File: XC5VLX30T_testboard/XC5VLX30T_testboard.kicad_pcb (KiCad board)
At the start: 4 copper layers, 15 parts, among them J1 Conn_02x30_Counter_Clockwise, J2 Conn_02x30_Counter_Clockwise, J3 Conn_02x30_Counter_Clockwise, J4 Conn_02x30_Counter_Clockwise, U1 XC5VLX30T-1FFG665C, X1 SG-5032CCN

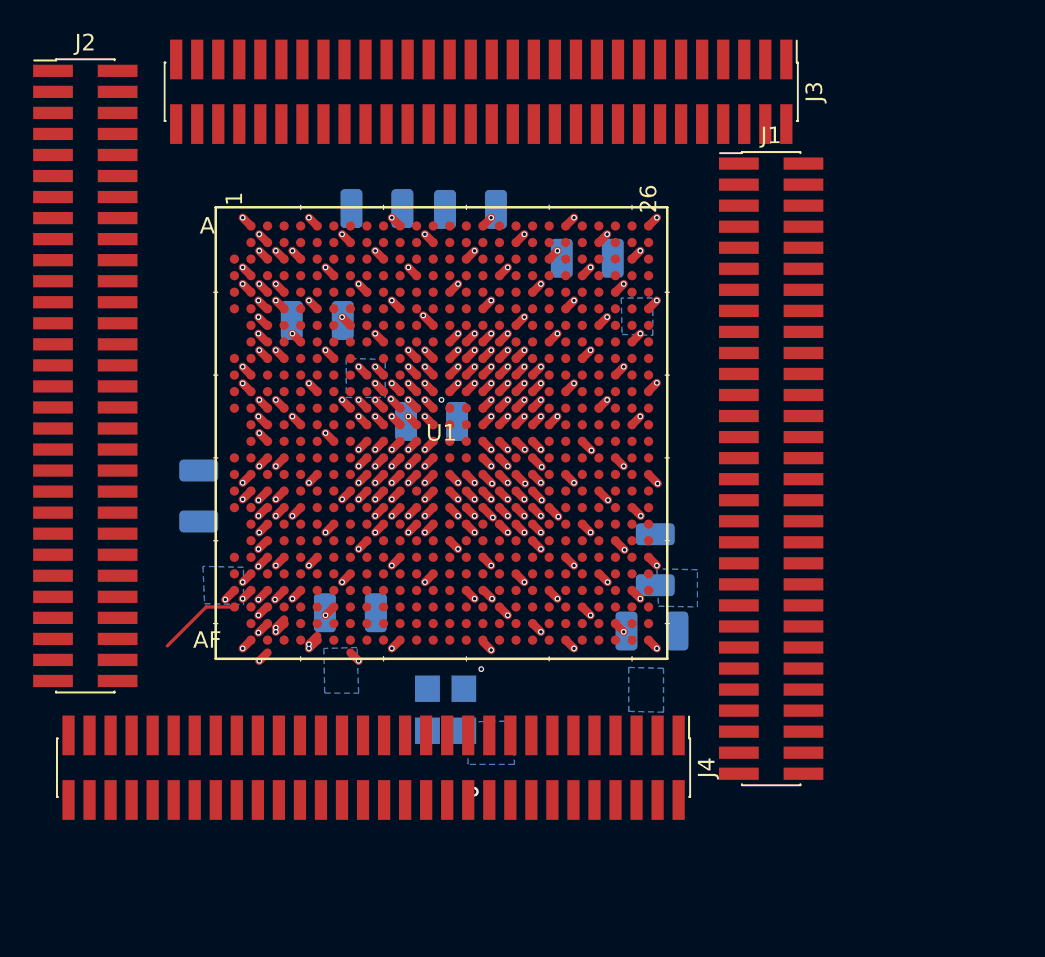
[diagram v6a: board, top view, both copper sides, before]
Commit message: routing
routed 240 pins on 4 layer
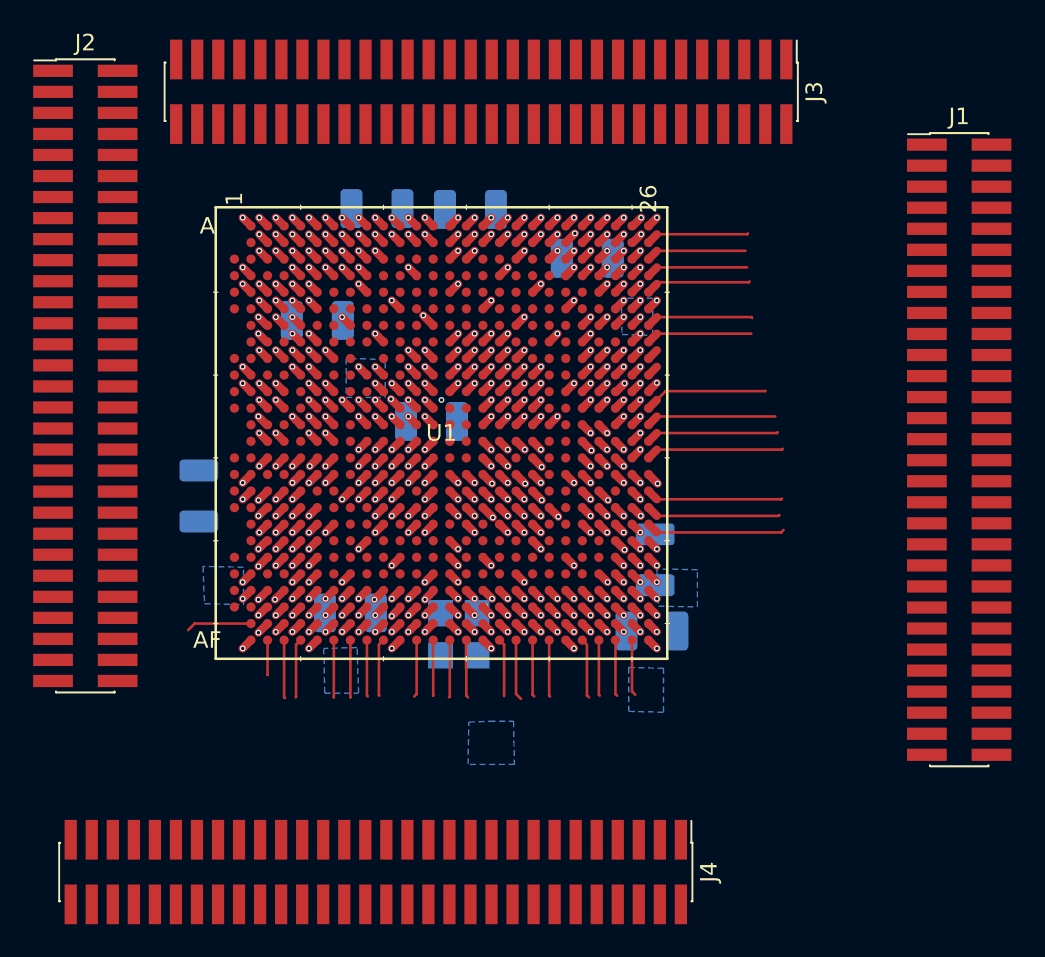
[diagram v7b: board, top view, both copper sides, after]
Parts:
- moved J1 11.4 mm to (192.9, 145.0)
- moved J4 6.30 mm to (157.7, 170.5)
- moved X1 4.62 mm to (162.7, 156.2)
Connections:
- U1 pad AC1: GND -> unconnected-(U1C-MGTRXN1_118-PadAC1)
- U1 pad AE10: unconnected-(U1G-IO_L4N_VREF_18-PadAE10) -> IO_L4N_VREF_18
- U1 pad AE11: unconnected-(U1G-IO_L2P_18-PadAE11) -> IO_L2P_18
- U1 pad AE12: unconnected-(U1G-IO_L0N_18-PadAE12) -> IO_L0N_18
- U1 pad AE13: unconnected-(U1G-IO_L18N_17-PadAE13) -> IO_L18N_17
- U1 pad AE15: unconnected-(U1G-IO_L16N_17-PadAE15) -> IO_L16N_17
- U1 pad AE16: unconnected-(U1G-IO_L15P_17-PadAE16) -> IO_L15P_17
- U1 pad AE17: unconnected-(U1G-IO_L14P_17-PadAE17) -> IO_L14P_17
- U1 pad AE18: unconnected-(U1G-IO_L13P_17-PadAE18) -> IO_L13P_17
- U1 pad AE20: unconnected-(U1G-IO_L9N_CC_17-PadAE20) -> IO_L9N_CC_17
- U1 pad AE21: unconnected-(U1G-IO_L8N_CC_17-PadAE21) -> IO_L8N_CC_17
- U1 pad AE22: unconnected-(U1G-IO_L5P_17-PadAE22) -> IO_L5P_17
- U1 pad AE23: unconnected-(U1G-IO_L4N_VREF_17-PadAE23) -> IO_L4N_VREF_17
- U1 pad AE25: unconnected-(U1G-IO_L2P_17-PadAE25) -> IO_L2P_17
- U1 pad AE26: unconnected-(U1G-IO_L2N_17-PadAE26) -> IO_L2N_17
- U1 pad AE5: unconnected-(U1C-IO_L14P_18-PadAE5) -> IO_L14P_18
- U1 pad AE6: unconnected-(U1C-IO_L13P_18-PadAE6) -> IO_L13P_18
- U1 pad AE7: unconnected-(U1C-IO_L11N_CC_18-PadAE7) -> IO_L11N_CC_18
- U1 pad AE8: unconnected-(U1C-IO_L11P_CC_18-PadAE8) -> IO_L11P_CC_18
- U1 pad AF10: unconnected-(U1G-IO_L6N_18-PadAF10) -> IO_L6N_18
- U1 pad AF12: unconnected-(U1G-IO_L0P_18-PadAF12) -> IO_L0P_18
- U1 pad AF13: unconnected-(U1G-IO_L18P_17-PadAF13) -> IO_L0P_17
- U1 pad AF14: unconnected-(U1G-IO_L17N_17-PadAF14) -> IO_L17N_17
- U1 pad AF15: unconnected-(U1G-IO_L17P_17-PadAF15) -> IO_L17P_17
- U1 pad AF17: unconnected-(U1G-IO_L14N_VREF_17-PadAF17) -> IO_L14N_VREF_17
- U1 pad AF18: unconnected-(U1G-IO_L12N_VRP_17-PadAF18) -> IO_L12N_VRP_17
- U1 pad AF19: unconnected-(U1G-IO_L12P_VRN_17-PadAF19) -> IO_L12P_VRN_17
- U1 pad AF20: unconnected-(U1G-IO_L9P_CC_17-PadAF20) -> IO_L9P_CC_17
- U1 pad AF22: unconnected-(U1G-IO_L8P_CC_17-PadAF22) -> IO_L8P_CC_17
- U1 pad AF23: unconnected-(U1G-IO_L4P_17-PadAF23) -> IO_L4P_17
- U1 pad AF24: unconnected-(U1G-IO_L3N_17-PadAF24) -> IO_L3N_17
- U1 pad AF25: unconnected-(U1G-IO_L3P_17-PadAF25) -> IO_L3P_17
- U1 pad AF3: unconnected-(U1C-IO_L15N_18-PadAF3) -> IO_L15N_18
- U1 pad AF4: unconnected-(U1C-IO_L15P_18-PadAF4) -> IO_L15P_18
- U1 pad AF5: unconnected-(U1C-IO_L13N_18-PadAF5) -> IO_L13N_18
- U1 pad AF7: unconnected-(U1C-IO_L8P_CC_18-PadAF7) -> IO_L8P_CC_18
- U1 pad AF8: unconnected-(U1C-IO_L8N_CC_18-PadAF8) -> IO_L8N_CC_18
- U1 pad AF9: unconnected-(U1C-IO_L6P_18-PadAF9) -> IO_L6P_18
- U1 pad F2: unconnected-(U1A-MGTTXN1_116-PadF2) -> GND
- U1 pad L3: unconnected-(U1A-MGTAVCC_112-PadL3) -> VccINT
- U1 pad L4: unconnected-(U1A-MGTAVCC_112-PadL4) -> VccINT
- U1 pad P5: GND -> unconnected-(U1B-MGTAVTTRXC-PadP5)
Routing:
- net VCCO: track 31.8 -> 134.5 mm
- net unconnected-(U1F-IO_L5N_SM4N_13-PadT25): track 0.00 -> 46.7 mm, vias 0 -> 5
- net unconnected-(U1B-IO_L8N_CC_12-PadT8): track 0.00 -> 41.3 mm, vias 0 -> 5
- net unconnected-(U1F-IO_L4P_13-PadU26): track 0.00 -> 24.8 mm, vias 0 -> 1
- net unconnected-(U1C-IO_L16N_15-PadC24): track 0.00 -> 20.2 mm, vias 0 -> 2
- net unconnected-(U1E-IO_L2P_SM6P_13-PadP24): track 0.00 -> 16.0 mm, vias 0 -> 2
- net unconnected-(U1D-IO_L16P_15-PadD24): track 0.00 -> 15.3 mm, vias 0 -> 2
- net unconnected-(U1F-IO_L8P_CC_SM1P_13-PadW26): track 0.00 -> 15.3 mm
- net unconnected-(U1F-IO_L4N_VREF_13-PadV26): track 0.00 -> 15.0 mm, vias 0 -> 1
- net unconnected-(U1C-IO_L12N_VRP_18-PadAD5): track 0.00 -> 14.5 mm, vias 0 -> 1
- net unconnected-(U1F-IO_L0N_SM8N_13-PadR26): track 0.00 -> 14.2 mm
- net unconnected-(U1E-IO_L0P_SM8P_13-PadP26): track 0.00 -> 13.8 mm
- net unconnected-(U1E-IO_L16P_SM12P_11-PadN26): track 0.00 -> 13.0 mm
- net unconnected-(U1E-IO_L16N_SM12N_11-PadM26): track 0.00 -> 12.9 mm
- net unconnected-(U1C-IO_L9N_CC_18-PadAB5): track 0.00 -> 12.5 mm, vias 0 -> 1
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- removed copper zone on In1.Cu, net VCCO
- removed copper zone on In1.Cu, net VccINT

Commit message: plumbing
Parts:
- added J5: Conn_01x35_Pin, Connector_PinHeader_1.27mm:PinHeader_1x35_P1.27mm_Vertical, F.Cu at (212.8, 102.6)
- added J6: Conn_01x35_Pin, Connector_PinHeader_1.27mm:PinHeader_1x35_P1.27mm_Vertical, F.Cu at (212.8, 148.2)
- added J7: Conn_01x35_Pin, Connector_PinHeader_1.27mm:PinHeader_1x35_P1.27mm_Vertical, F.Cu at (164.6, 193.1)
- added J8: Conn_01x35_Pin, Connector_PinHeader_1.27mm:PinHeader_1x35_P1.27mm_Vertical, F.Cu at (210.2, 193.0)
- J1, J2, J3, J4: value Conn_02x30_Counter_Clockwise -> Conn_01x35_Pin; footprint Connector_PinHeader_1.27mm:PinHeader_2x30_P1.27mm_Vertical_SMD -> Connector_PinHeader_1.27mm:PinHeader_1x35_P1.27mm_Vertical
- moved J1 86.1 mm to (118.2, 102.0)
- moved J4 71.6 mm to (167.1, 99.5), turned to 90 degrees
- moved J3 48.7 mm to (121.6, 99.5), turned to 90 degrees
- moved J2 23.0 mm to (118.3, 147.6)
- moved U1 4.13 mm to (164.4, 147.1)
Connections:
- J3 pad 2: unconnected-(J3-Pin_2-Pad2) -> J5PIN1
- J3 pad 3: unconnected-(J3-Pin_3-Pad3) -> J5PIN1
- J3 pad 4: unconnected-(J3-Pin_4-Pad4) -> J5PIN1
- J3 pad 5: unconnected-(J3-Pin_5-Pad5) -> IO_L14P_16
- J3 pad 6: unconnected-(J3-Pin_6-Pad6) -> IO_L14P_16
- U1 pad A4: unconnected-(U1A-IO_L14P_16-PadA4) -> IO_L14P_16
- U1 pad AA16: VCCO -> unconnected-(U1F-IO_L4P_13-PadU26)
- U1 pad AA6: VCCO -> unconnected-(U1F-IO_L4P_13-PadU26)
- U1 pad AB13: VCCO -> unconnected-(U1F-IO_L4P_13-PadU26)
- U1 pad AB23: VCCO -> unconnected-(U1F-IO_L4P_13-PadU26)
- U1 pad AC10: VCCO -> unconnected-(U1F-IO_L4P_13-PadU26)
- U1 pad AC20: VCCO -> unconnected-(U1F-IO_L4P_13-PadU26)
- U1 pad B13: VCCO -> unconnected-(U1F-IO_L4P_13-PadU26)
- U1 pad B23: VCCO -> unconnected-(U1F-IO_L4P_13-PadU26)
- U1 pad B4: unconnected-(U1A-IO_L16P_16-PadB4) -> IO_L16P_16
- U1 pad C10: VCCO -> unconnected-(U1F-IO_L4P_13-PadU26)
- U1 pad C23: unconnected-(U1C-IO_L15N_15-PadC23) -> unconnected-(U1F-IO_L4P_13-PadU26)
- U1 pad D17: VCCO -> unconnected-(U1F-IO_L4P_13-PadU26)
- U1 pad D23: unconnected-(U1D-IO_L12P_VRN_15-PadD23) -> unconnected-(U1F-IO_L4P_13-PadU26)
- U1 pad D7: VCCO -> unconnected-(U1F-IO_L4P_13-PadU26)
- U1 pad E14: VCCO -> unconnected-(U1F-IO_L4P_13-PadU26)
- U1 pad E24: VCCO -> unconnected-(U1F-IO_L4P_13-PadU26)
- U1 pad E6: unconnected-(U1A-IO_L7P_16-PadE6) -> IO_L7P_16
- U1 pad F11: VCCO -> unconnected-(U1F-IO_L4P_13-PadU26)
- U1 pad F21: VCCO -> unconnected-(U1F-IO_L4P_13-PadU26)
- U1 pad G18: VCCO -> unconnected-(U1F-IO_L4P_13-PadU26)
- U1 pad G8: VCCO -> unconnected-(U1F-IO_L4P_13-PadU26)
- U1 pad H25: VCCO -> unconnected-(U1F-IO_L4P_13-PadU26)
- U1 pad H5: VCCO -> unconnected-(U1F-IO_L4P_13-PadU26)
- U1 pad H6: unconnected-(U1A-IO_L1N_12-PadH6) -> unconnected-(U1F-IO_L4P_13-PadU26)
- U1 pad J12: VCCO -> unconnected-(U1F-IO_L4P_13-PadU26)
- U1 pad J22: VCCO -> unconnected-(U1F-IO_L4P_13-PadU26)
- U1 pad J6: unconnected-(U1A-IO_L7N_12-PadJ6) -> unconnected-(U1F-IO_L4P_13-PadU26)
- U1 pad K6: unconnected-(U1A-IO_L10P_CC_12-PadK6) -> unconnected-(U1F-IO_L4P_13-PadU26)
- U1 pad L25: unconnected-(U1E-IO_L14N_VREF_11-PadL25) -> IO_L14N_VREF_11
- U1 pad L6: VCCO -> unconnected-(U1F-IO_L4P_13-PadU26)
- U1 pad M22: unconnected-(U1E-IO_L19N_SM9N_11-PadM22) -> unconnected-(U1F-IO_L4P_13-PadU26)
- U1 pad M23: VCCO -> unconnected-(U1F-IO_L4P_13-PadU26)
- U1 pad M7: unconnected-(U1B-IO_L14P_12-PadM7) -> unconnected-(U1F-IO_L4P_13-PadU26)
- U1 pad N23: unconnected-(U1E-IO_L18N_SM10N_11-PadN23) -> unconnected-(U1F-IO_L4P_13-PadU26)
- U1 pad N7: unconnected-(U1B-IO_L17N_12-PadN7) -> unconnected-(U1F-IO_L4P_13-PadU26)
- U1 pad P23: unconnected-(U1E-IO_L2N_SM6N_13-PadP23) -> unconnected-(U1F-IO_L4P_13-PadU26)
- U1 pad P7: VCCO -> unconnected-(U1F-IO_L4P_13-PadU26)
- U1 pad R23: unconnected-(U1E-IO_L3P_SM5P_13-PadR23) -> unconnected-(U1F-IO_L4P_13-PadU26)
- U1 pad R24: VCCO -> unconnected-(U1F-IO_L4P_13-PadU26)
- U1 pad R7: unconnected-(U1B-IO_L19N_12-PadR7) -> unconnected-(U1F-IO_L4P_13-PadU26)
- U1 pad T7: unconnected-(U1B-IO_L15N_12-PadT7) -> unconnected-(U1F-IO_L4P_13-PadU26)
- U1 pad V23: unconnected-(U1F-IO_L9N_CC_SM0N_13-PadV23) -> unconnected-(U1F-IO_L4P_13-PadU26)
- U1 pad V25: VCCO -> unconnected-(U1F-IO_L4P_13-PadU26)
- U1 pad W22: VCCO -> unconnected-(U1F-IO_L4P_13-PadU26)
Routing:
- net unconnected-(U1F-IO_L4P_13-PadU26): track 24.8 -> 272.2 mm, vias 1 -> 43
- net VCCO: track 134.5 -> 2.83 mm, vias 31 -> 4
- net IO_L14P_16: track 0.00 -> 54.2 mm, vias 0 -> 3
- net unconnected-(U1B-IO_L8N_CC_12-PadT8): track 41.3 -> 0.00 mm, vias 5 -> 0
- net J5PIN1: track 0.00 -> 39.5 mm, vias 0 -> 3
- net unconnected-(U1F-IO_L5N_SM4N_13-PadT25): track 46.7 -> 7.64 mm, vias 5 -> 1
- net unconnected-(U1A-IO_L10N_CC_16-PadB7): track 3.70 -> 42.2 mm
- net IO_L7P_16: track 0.00 -> 35.9 mm, vias 0 -> 2
- net IO_L16P_16: track 0.00 -> 29.5 mm, vias 0 -> 1
- net unconnected-(U1A-IO_L14N_VREF_16-PadA3): track 2.89 -> 28.5 mm
- net unconnected-(U1A-IO_L16N_16-PadB5): track 3.89 -> 28.6 mm
- net unconnected-(U1A-IO_L12N_VRP_16-PadA5): track 2.63 -> 27.3 mm
- net unconnected-(U1A-IO_L12P_VRN_16-PadB6): track 3.79 -> 28.0 mm
- net unconnected-(U1A-IO_L7N_16-PadD6): track 6.27 -> 30.4 mm, vias 1 -> 2
- net unconnected-(U1A-IO_L9N_CC_16-PadC6): track 4.91 -> 29.0 mm, vias 1 -> 2
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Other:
- board text added: "33 i/o"
- board text added: "49 i/o"
- board text added: "70 i/o"
- board text added: "72 i/o"
